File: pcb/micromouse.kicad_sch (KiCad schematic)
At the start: 25 parts, among them J1 AVR-ISP-6, J2 Conn_01x02, J4 Conn_01x02, J5 Conn_01x04, Q1 Si2319CDS, U1 TSSP77038ETR, U2 TSSP77038ETR, U3 TSSP77038ETR, U4 TSSP77038ETR, U5 TSSP77038ETR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

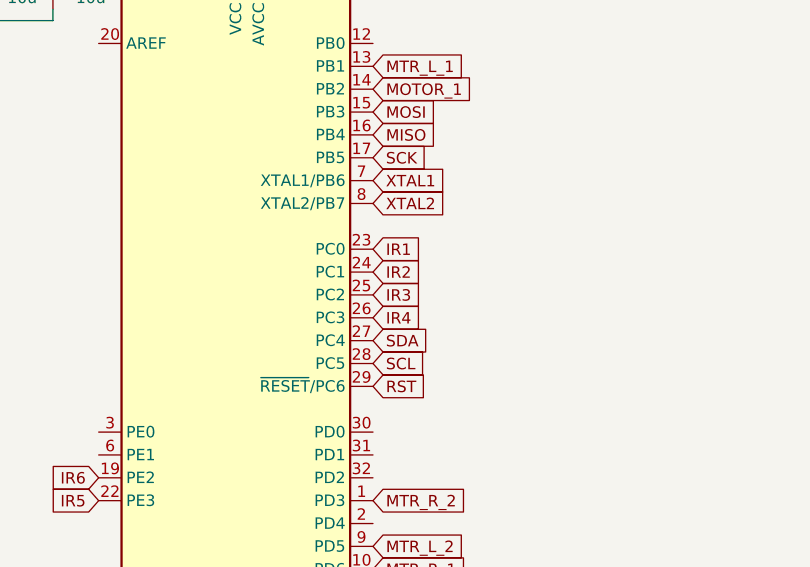
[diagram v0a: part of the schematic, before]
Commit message: remake IR wiring
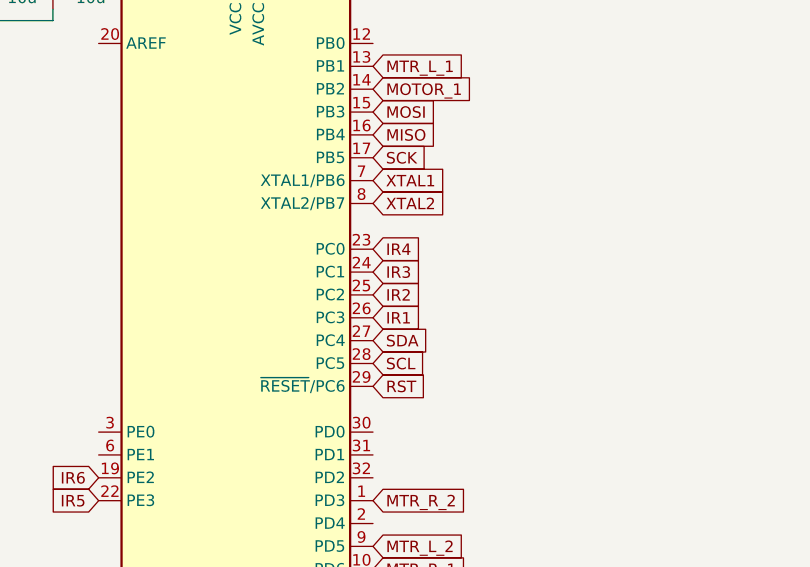
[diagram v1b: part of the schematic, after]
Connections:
- net IR1: now also U7.26 (PC3); no longer U7.23 (PC0)
- net IR2: now also U7.25 (PC2); no longer U7.24 (PC1)
- net IR3: now also U7.24 (PC1); no longer U7.25 (PC2)
- net IR4: now also U7.23 (PC0); no longer U7.26 (PC3)

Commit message: update link
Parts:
- added C10, C7, C9: 10u, Capacitor_SMD:C_0603_1608Metric, symbol Device:C_Small
- added J2: Conn_01x02, Connector_PinSocket_2.54mm:PinSocket_1x02_P2.54mm_Vertical, symbol Connector_Generic:Conn_01x02
- added U9: LM317_SOT-223, Package_TO_SOT_SMD:SOT-223-3_TabPin2, symbol Regulator_Linear:LM317_SOT-223
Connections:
- net +3.3V: now also C10.1, C9.1, U9.2 (VO)
- net +BATT: now also C7.1, J2.2 (Pin_2), U9.3 (VI)
- net GND: now also C10.2, C7.2, C9.2, J2.1 (Pin_1), U9.1 (ADJ)

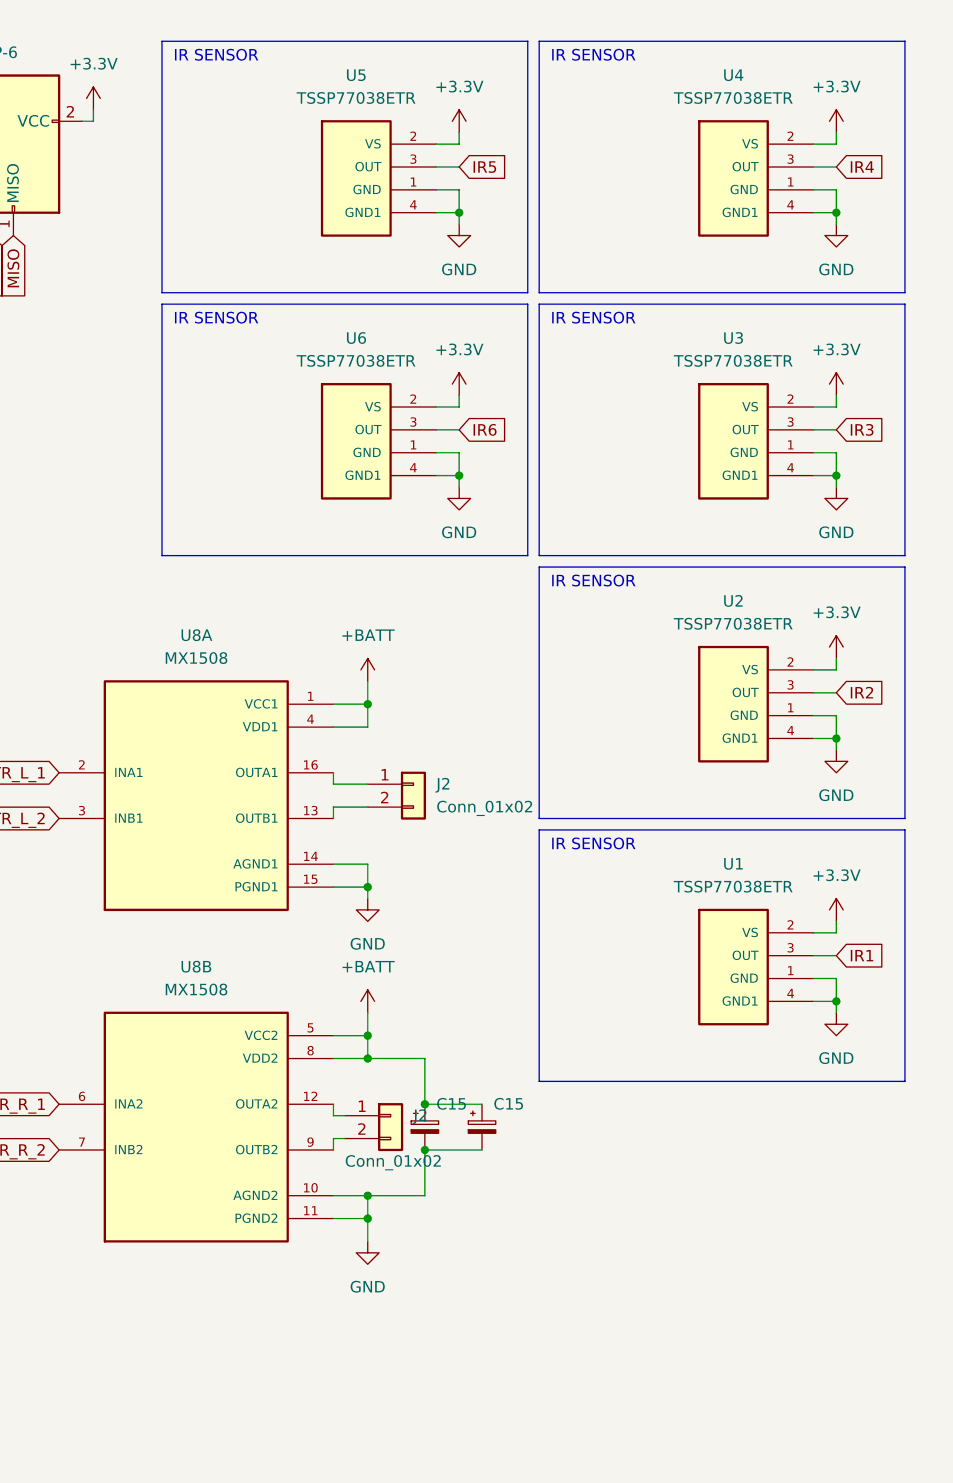
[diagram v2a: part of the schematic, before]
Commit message: update ir sensor
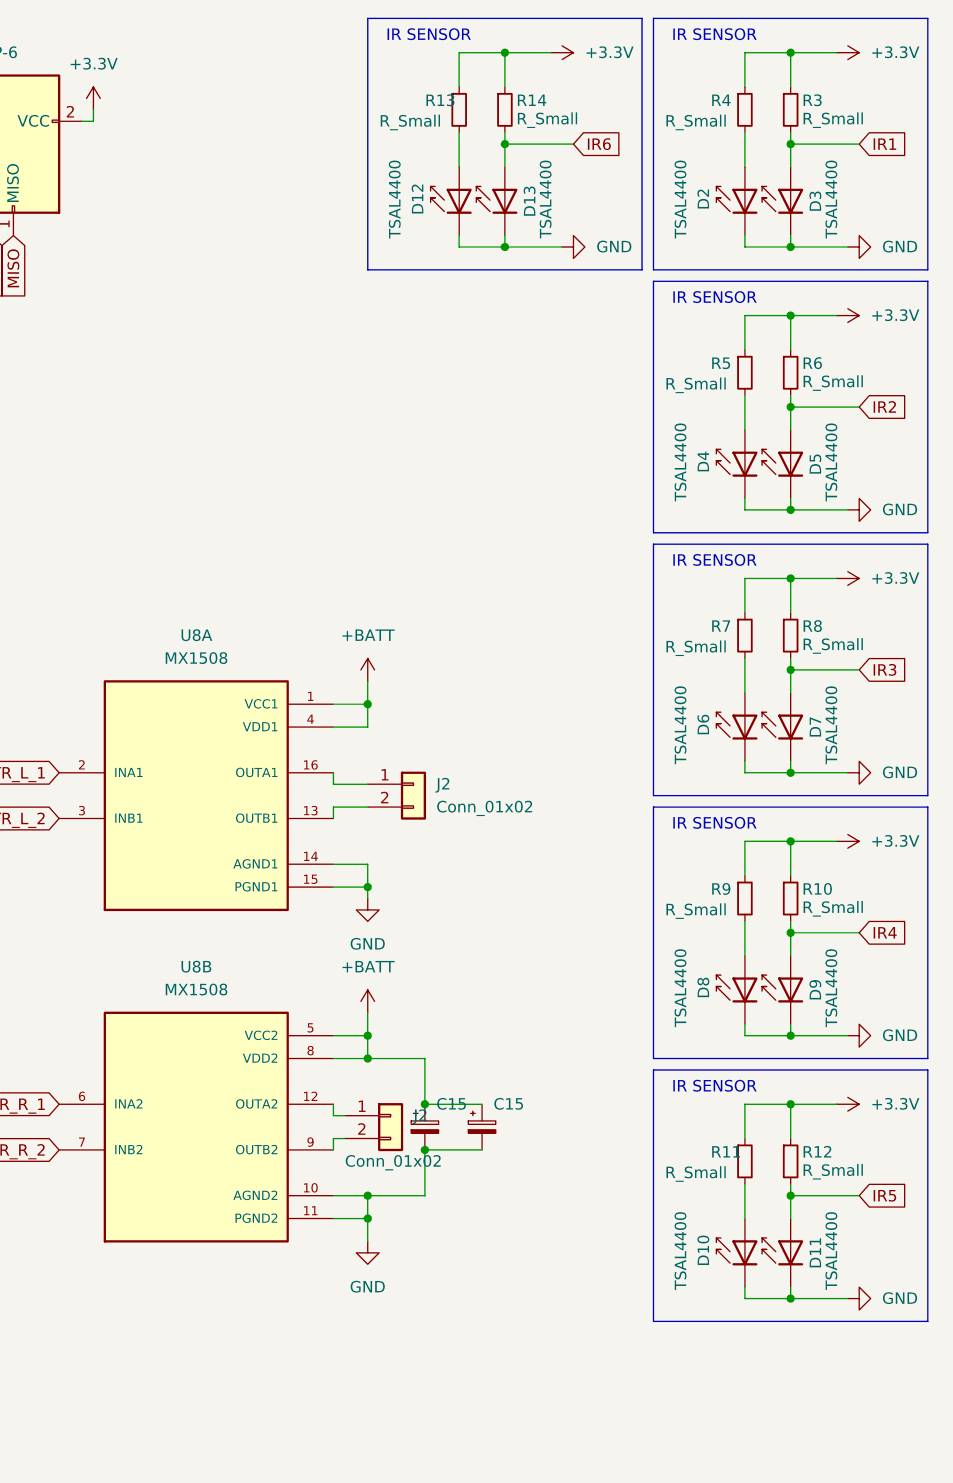
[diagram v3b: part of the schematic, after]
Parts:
- removed U1, U2, U3, U4, U5, U6: TSSP77038ETR, Library:TSSP77, symbol TSSP77:TSSP77038ETR
- added D10, D11, D12, D13, D2, D3, D4, D5, D6, D7, D8, D9: TSAL4400, LED_THT:LED_D3.0mm_IRBlack, symbol LED:TSAL4400
- added R10, R11, R12, R13, R14, R3, R4, R5, R6, R7, R8, R9: R_Small, Resistor_SMD:R_0603_1608Metric, symbol Device:R_Small
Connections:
- net +3.3V: now also R10.1, R11.1, R12.1, R13.1, R14.1, R3.1, R4.1, R5.1, R6.1, R7.1, R8.1, R9.1
- net GND: now also D10.1 (K), D11.1 (K), D12.1 (K), D13.1 (K), D2.1 (K), D3.1 (K), D4.1 (K), D5.1 (K), D6.1 (K), D7.1 (K), D8.1 (K), D9.1 (K)
- net IR1: now also D3.2 (A), R3.2
- net IR2: now also D5.2 (A), R6.2
- net IR3: now also D7.2 (A), R8.2
- net IR4: now also D9.2 (A), R10.2
- net IR5: now also D11.2 (A), R12.2
- net IR6: now also D13.2 (A), R14.2
- new net: D4.2 (A), R5.2
- new net: D6.2 (A), R7.2
- new net: D12.2 (A), R13.2
- new net: D10.2 (A), R11.2
- new net: D8.2 (A), R9.2
- new net: D2.2 (A), R4.2
